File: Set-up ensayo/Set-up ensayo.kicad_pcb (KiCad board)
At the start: 2 copper layers, 53.3 x 61 mm, 17 parts, among them J1 Conn_Coaxial, J2 DB9_Female_MountingHoles

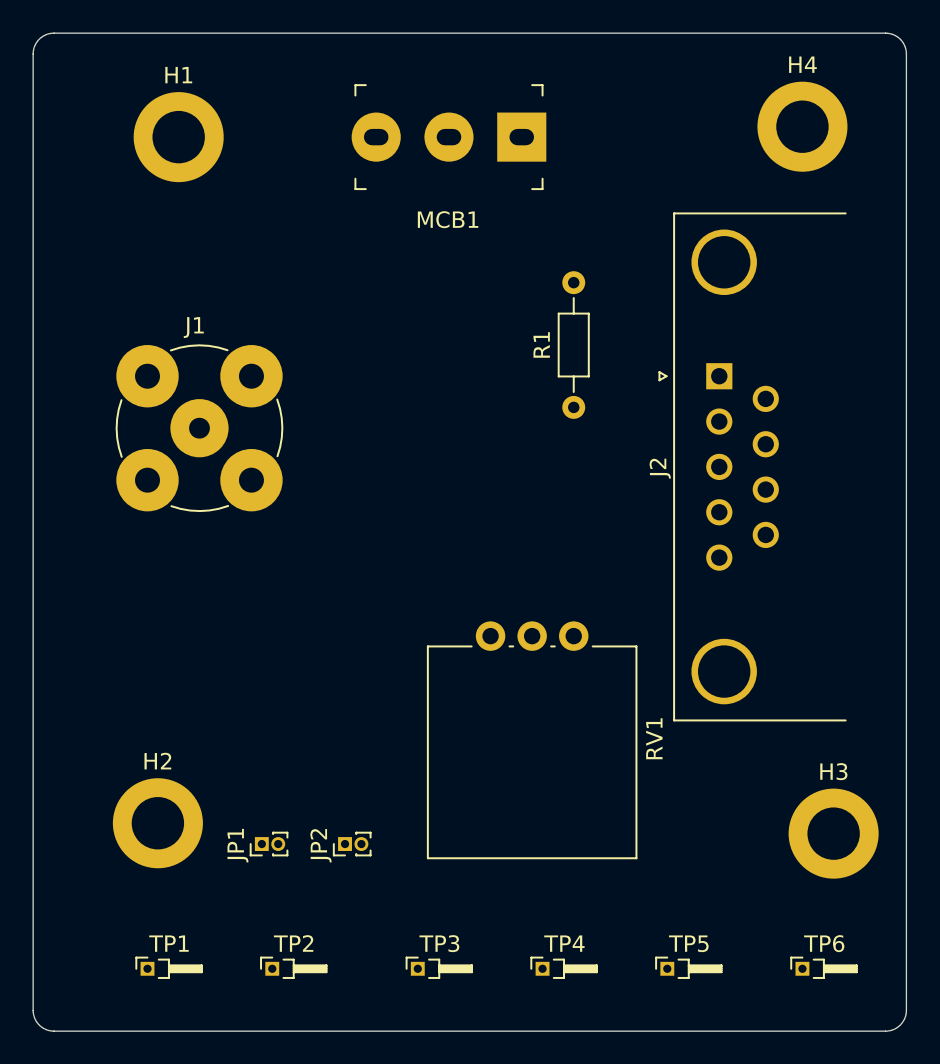
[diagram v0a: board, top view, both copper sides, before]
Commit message: Terminé 2do y 3er paso en proceso de diseño de PCB
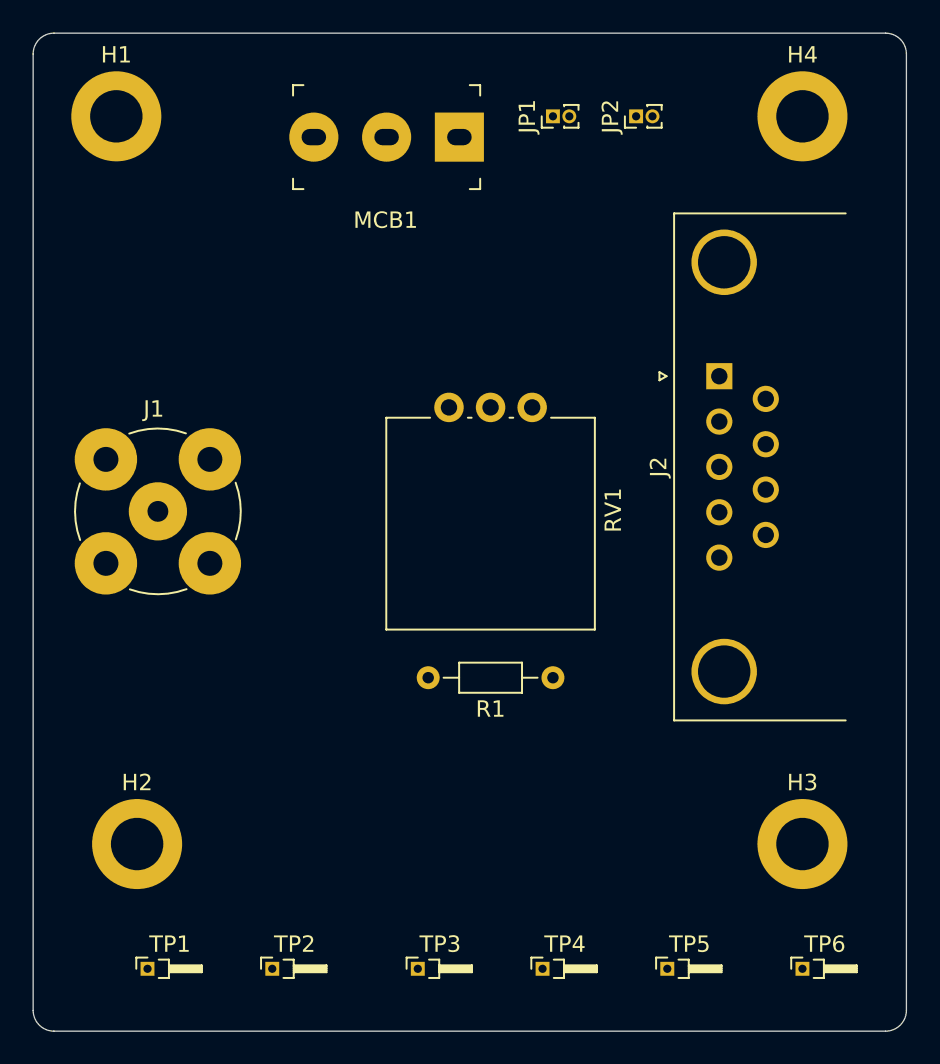
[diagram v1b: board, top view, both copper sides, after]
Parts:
- moved JP1 47.9 mm to (128.3, 80.0)
- moved JP2 47.9 mm to (133.3, 80.0)
- moved R1 16.6 mm to (128.3, 114.3), turned to 180 degrees
- moved RV1 14.2 mm to (121.9, 97.8)
- moved J1 5.68 mm to (104.1, 104.1)
- moved H1 4.02 mm to (101.6, 80.0)
- moved MCB1 3.81 mm to (118.1, 81.3)
- moved H3 2.01 mm to (143.5, 124.5)
- moved H2 1.80 mm to (102.9, 124.5)
- moved H4 0.63 mm to (143.5, 80.0)
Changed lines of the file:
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@@
   )
   (module "Footprints proyecto:PinHeader_1x02_P1.00mm_Vertical" (layer F.Cu)
-    (at 115.57 124.46 90)
+    (at 133.35 80.01 90)
     (descr "Through hole straight pin header, 1x02, 1.00mm pitch, single row")
     (tags "Through hole pin header THT 1x02 1.00mm single row")
@@
   )
   (module "Footprints proyecto:PinHeader_1x02_P1.00mm_Vertical" (layer F.Cu)
-    (at 110.49 124.46 90)
+    (at 128.27 80.01 90)
     (descr "Through hole straight pin header, 1x02, 1.00mm pitch, single row")
     (tags "Through hole pin header THT 1x02 1.00mm single row")
@@
   )
   (module "Footprints proyecto:Potentiometer_Vishay_248GJ-249GJ_Single_Vertical" (layer F.Cu)
-    (at 124.46 111.76 270)
+    (at 121.92 97.79 270)
     (descr "Potentiometer, vertical, Vishay 248GJ-249GJ Single, http://www.vishay.com/docs/57054/248249.pdf")
     (tags "Potentiometer vertical Vishay 248GJ-249GJ Single")
@@
   )
   (module "Footprints proyecto:MountingHole_3.2mm_M3_ISO14580_Pad" (layer F.Cu)
-    (at 105.41 81.28)
+    (at 101.6 80.01)
     (descr "Mounting Hole 3.2mm, M3, ISO14580")
     (tags "mounting hole 3.2mm m3 iso14580")
@@
   )
   (module "Footprints proyecto:MountingHole_3.2mm_M3_ISO14580_Pad" (layer F.Cu)
-    (at 104.14 123.19)
+    (at 102.87 124.46)
     (descr "Mounting Hole 3.2mm, M3, ISO14580")
     (tags "mounting hole 3.2mm m3 iso14580")
@@
   )
   (module "Footprints proyecto:MountingHole_3.2mm_M3_ISO14580_Pad" (layer F.Cu)
-    (at 145.415 123.825)
+    (at 143.51 124.46)
     (descr "Mounting Hole 3.2mm, M3, ISO14580")
     (tags "mounting hole 3.2mm m3 iso14580")
@@
   )
   (module "Footprints proyecto:MountingHole_3.2mm_M3_ISO14580_Pad" (layer F.Cu)
-    (at 143.51 80.645)
+    (at 143.51 80.01)
     (descr "Mounting Hole 3.2mm, M3, ISO14580")
     (tags "mounting hole 3.2mm m3 iso14580")
@@
   )
   (module "Footprints proyecto:BNC_TEConnectivity_1478204_Vertical" (layer F.Cu)
-    (at 106.68 99.06)
+    (at 104.14 104.14)
     (descr "BNC female PCB mount 4 pin straight chassis connector http://www.te.com/usa-en/product-1-1478204-0.html")
     (tags "BNC female PCB mount 4 pin straight chassis connector ")
@@
   )
   (module "Footprints proyecto:Switch_Toggle_ATE1D-2M3-10-Z" (layer F.Cu)
-    (at 121.92 81.28 180)
+    (at 118.11 81.28 180)
     (descr https://www.nidec-copal-electronics.com/e/catalog/switch/ate.pdf)
     (fp_text reference MCB1 (at 0.06 -5.08) (layer F.SilkS)
@@
   )
   (module "Footprints proyecto:R_Axial_DIN0204_L3.6mm_D1.6mm_P7.62mm_Horizontal" (layer F.Cu)
-    (at 129.54 97.79 90)
+    (at 128.27 114.3 180)
     (descr "Resistor, Axial_DIN0204 series, Axial, Horizontal, pin pitch=7.62mm, 0.167W, length*diameter=3.6*1.6mm^2, http://cdn-reichelt.de/documents/datenblatt/B400/1_4W%23YAG.pdf")
     (tags "Resistor Axial_DIN0204 series Axial Horizontal pin pitch 7.62mm 0.167W length 3.6mm diameter 1.6mm")
-    (fp_text reference R1 (at 3.81 -1.92 90) (layer F.SilkS)
-      (effects (font (size 1 1) (thickness 0.15)))
-    )
-    (fp_text value 15k (at 3.81 1.92 90) (layer F.Fab)
+    (fp_text reference R1 (at 3.81 -1.92) (layer F.SilkS)
+      (effects (font (size 1 1) (thickness 0.15)))
+    )
+    (fp_text value 15k (at 3.81 1.92) (layer F.Fab)
       (effects (font (size 1 1) (thickness 0.15)))
     )
@@
     (fp_line (start 8.57 1.05) (end 8.57 -1.05) (layer F.CrtYd) (width 0.05))
     (fp_line (start 8.57 -1.05) (end -0.95 -1.05) (layer F.CrtYd) (width 0.05))
-    (fp_text user %R (at 3.81 0 90) (layer F.Fab)
+    (fp_text user %R (at 3.81 0) (layer F.Fab)
       (effects (font (size 0.72 0.72) (thickness 0.108)))
     )
-    (pad 1 thru_hole circle (at 0 0 90) (size 1.4 1.4) (drill 0.7) (layers *.Cu *.Mask)
+    (pad 1 thru_hole circle (at 0 0 180) (size 1.4 1.4) (drill 0.7) (layers *.Cu *.Mask)
       (net 13 "Net-(JP1-Pad2)"))
-    (pad 2 thru_hole oval (at 7.62 0 90) (size 1.4 1.4) (drill 0.7) (layers *.Cu *.Mask)
+    (pad 2 thru_hole oval (at 7.62 0 180) (size 1.4 1.4) (drill 0.7) (layers *.Cu *.Mask)
       (net 4 /VZs1))
     (model ${KISYS3DMOD}/Resistor_THT.3dshapes/R_Axial_DIN0204_L3.6mm_D1.6mm_P7.62mm_Horizontal.wrl

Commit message: Comencé con el paso 4 del proceso de diseño de PCB pero debo verificar el footprint de los pines, creo que es un footprint muy chico
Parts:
- moved R1 7.73 mm to (120.7, 115.6), turned to 0 degrees
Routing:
- net /VAC: track 0.00 -> 76.1 mm
- net /VZs1: track 0.00 -> 52.0 mm
- net Net-(JP1-Pad2): track 0.00 -> 39.0 mm
- net Net-(JP2-Pad2): track 0.00 -> 22.2 mm
- net /Vi: track 0.00 -> 6.12 mm
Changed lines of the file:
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@@
     (thickness 1.6)
     (drawings 8)
-    (tracks 0)
+    (tracks 32)
     (zones 0)
     (modules 17)
@@
   )
   (module "Footprints proyecto:R_Axial_DIN0204_L3.6mm_D1.6mm_P7.62mm_Horizontal" (layer F.Cu)
-    (at 128.27 114.3 180)
+    (at 120.65 115.57)
     (descr "Resistor, Axial_DIN0204 series, Axial, Horizontal, pin pitch=7.62mm, 0.167W, length*diameter=3.6*1.6mm^2, http://cdn-reichelt.de/documents/datenblatt/B400/1_4W%23YAG.pdf")
     (tags "Resistor Axial_DIN0204 series Axial Horizontal pin pitch 7.62mm 0.167W length 3.6mm diameter 1.6mm")
@@
       (effects (font (size 0.72 0.72) (thickness 0.108)))
     )
-    (pad 1 thru_hole circle (at 0 0 180) (size 1.4 1.4) (drill 0.7) (layers *.Cu *.Mask)
+    (pad 1 thru_hole circle (at 0 0) (size 1.4 1.4) (drill 0.7) (layers *.Cu *.Mask)
       (net 13 "Net-(JP1-Pad2)"))
-    (pad 2 thru_hole oval (at 7.62 0 180) (size 1.4 1.4) (drill 0.7) (layers *.Cu *.Mask)
+    (pad 2 thru_hole oval (at 7.62 0) (size 1.4 1.4) (drill 0.7) (layers *.Cu *.Mask)
       (net 4 /VZs1))
     (model ${KISYS3DMOD}/Resistor_THT.3dshapes/R_Axial_DIN0204_L3.6mm_D1.6mm_P7.62mm_Horizontal.wrl
@@
   (gr_line (start 97.79 135.89) (end 148.59 135.89) (layer Edge.Cuts) (width 0.05))
   (gr_line (start 96.52 76.2) (end 96.52 134.62) (layer Edge.Cuts) (width 0.05))
+  (segment (start 104.14 104.14) (end 104.14 91.44) (width 1) (layer B.Cu) (net 2))
+  (segment (start 104.14 91.44) (end 109.22 86.36) (width 1) (layer B.Cu) (net 2))
+  (segment (start 113.03 86.36) (end 118.11 81.28) (width 1) (layer B.Cu) (net 2))
+  (segment (start 109.22 86.36) (end 113.03 86.36) (width 1) (layer B.Cu) (net 2))
+  (segment (start 104.14 104.14) (end 104.14 116.84) (width 1) (layer B.Cu) (net 2))
+  (segment (start 104.14 116.84) (end 107.95 120.65) (width 1) (layer B.Cu) (net 2))
+  (segment (start 107.95 127.635) (end 103.505 132.08) (width 1) (layer B.Cu) (net 2))
+  (segment (start 107.95 120.65) (end 107.95 127.635) (width 1) (layer B.Cu) (net 2))
+  (segment (start 115.57 127.635) (end 120.015 132.08) (width 1) (layer B.Cu) (net 2))
+  (segment (start 107.95 127.635) (end 115.57 127.635) (width 1) (layer B.Cu) (net 2))
+  (segment (start 124.46 97.79) (end 127 97.79) (width 1) (layer B.Cu) (net 4))
+  (segment (start 127.865 98.655) (end 127 97.79) (width 1) (layer B.Cu) (net 4))
+  (segment (start 138.43 98.655) (end 127.865 98.655) (width 1) (layer B.Cu) (net 4))
+  (segment (start 128.27 115.57) (end 128.27 118.11) (width 1) (layer B.Cu) (net 4))
+  (segment (start 135.255 125.095) (end 135.255 132.08) (width 1) (layer B.Cu) (net 4))
+  (segment (start 128.27 118.11) (end 135.255 125.095) (width 1) (layer B.Cu) (net 4))
+  (segment (start 127 114.3) (end 128.27 115.57) (width 1) (layer B.Cu) (net 4))
+  (segment (start 127 97.79) (end 127 114.3) (width 1) (layer B.Cu) (net 4))
+  (segment (start 126.874999 81.28) (end 128.144999 80.01) (width 1) (layer B.Cu) (net 11))
+  (segment (start 122.555 81.28) (end 126.874999 81.28) (width 1) (layer B.Cu) (net 11))
+  (segment (start 120.65 115.57) (end 120.65 105.41) (width 1) (layer B.Cu) (net 13))
+  (segment (start 120.65 105.41) (end 118.11 102.87) (width 1) (layer B.Cu) (net 13))
+  (segment (start 118.11 102.87) (end 118.11 95.25) (width 1) (layer B.Cu) (net 13))
+  (segment (start 118.11 95.25) (end 124.46 88.9) (width 1) (layer B.Cu) (net 13))
+  (segment (start 124.46 88.9) (end 127 88.9) (width 1) (layer B.Cu) (net 13))
+  (segment (start 127 88.9) (end 129.54 86.36) (width 1) (layer B.Cu) (net 13))
+  (segment (start 129.54 86.36) (end 129.54 83.82) (width 1) (layer B.Cu) (net 13))
+  (segment (start 121.92 97.79) (end 121.92 96.52) (width 1) (layer B.Cu) (net 14))
+  (segment (start 121.92 96.52) (end 127 91.44) (width 1) (layer B.Cu) (net 14))
+  (segment (start 127 91.44) (end 132.08 91.44) (width 1) (layer B.Cu) (net 14))
+  (segment (start 132.08 91.44) (end 134.62 88.9) (width 1) (layer B.Cu) (net 14))
+  (segment (start 134.62 88.9) (end 134.62 83.82) (width 1) (layer B.Cu) (net 14))
 )

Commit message: Cambié los footprints pero son demasiado grandes para colocar los que son horizontales, los voy a cambiar por verticales
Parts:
- JP1, JP2: footprint Footprints proyecto:PinHeader_1x02_P1.00mm_Vertical -> Footprints proyecto:PinHeader_1x02_P2.54mm_Vertical
- TP1, TP2, TP3, TP4, TP5, TP6: footprint Footprints proyecto:PinHeader_1x01_P1.00mm_Horizontal -> Footprints proyecto:PinHeader_1x01_P2.54mm_Horizontal
- moved TP6 32.5 mm to (111.8, 125.1)
- moved TP5 11.3 mm to (126.4, 125.1)
- moved TP4 10.2 mm to (137.8, 132.1)
- moved TP3 5.08 mm to (125.1, 132.1)
- moved TP1 3.81 mm to (99.7, 132.1)
- moved JP2 2.01 mm to (135.3, 80.6)
- moved TP2 1.27 mm to (112.4, 132.1)
- moved JP1 0.90 mm to (128.9, 80.6)
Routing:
- net /VAC: track 76.1 -> 30.9 mm
- net /VZs1: track 52.0 -> 32.6 mm
- net /Vi: track 6.12 -> 0.00 mm

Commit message: Cambio de footprint horizontal por verticales para pines de medicion y ruteo de las pistas correspondientes
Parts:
- TP1, TP2, TP3, TP4, TP5, TP6: footprint Footprints proyecto:PinHeader_1x01_P2.54mm_Horizontal -> Footprints proyecto:PinHeader_1x01_P2.54mm_Vertical
- moved TP6 31.8 mm to (142.9, 131.4)
- moved TP5 10.9 mm to (135.3, 131.4)
- moved TP4 10.2 mm to (127.6, 131.4)
- moved TP1 5.12 mm to (104.8, 131.4)
- moved TP3 5.12 mm to (120.0, 131.4)
- moved TP2 0.64 mm to (112.4, 131.4)
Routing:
- net /VAC: track 30.9 -> 74.8 mm
- net /VZs1: track 32.6 -> 51.4 mm
- net /Vi: track 0.00 -> 16.2 mm
- net Net-(JP2-Pad2): track 22.2 -> 26.7 mm
- net Net-(JP1-Pad2): track 39.0 -> 43.0 mm

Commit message: 5to paso de proceso de diseño de PCB finalizado
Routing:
- added copper zone on B.Cu, net /GND
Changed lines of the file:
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@@
   (segment (start 137.795 83.185) (end 137.795 80.645) (width 1) (layer B.Cu) (net 14))
   (segment (start 134.62 86.36) (end 137.795 83.185) (width 1) (layer B.Cu) (net 14))
+  (zone (net 1) (net_name /GND) (layer B.Cu) (hatch edge 0.508)
+    (connect_pads (clearance 0.508))
+    (min_thickness 0.254)
+    (fill yes (arc_segments 32) (thermal_gap 0.508) (thermal_bridge_width 0.508))
+    (polygon
+      (pts
+        (xy 97.155 75.565) (xy 149.225 75.565) (xy 149.225 135.255) (xy 97.155 135.255)
+      )
+    )
+  )
 )
